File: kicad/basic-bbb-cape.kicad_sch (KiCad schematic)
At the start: 3 parts, among them J8 BBB_P8, J9 BBB_P9, U1 CAT24C32YI-GT3

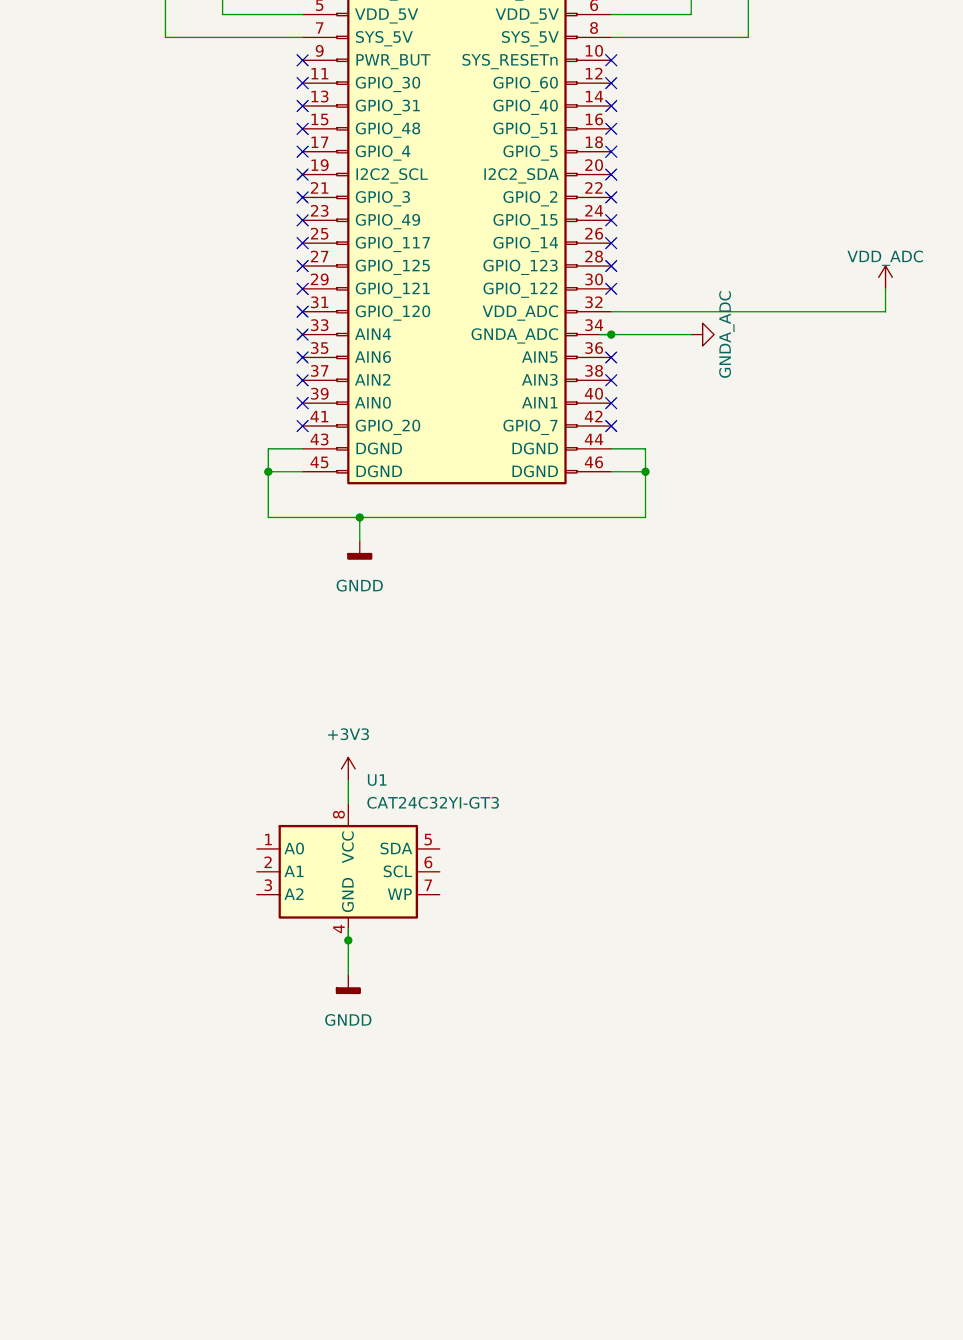
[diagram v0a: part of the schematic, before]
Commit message: Add resistor pack/network
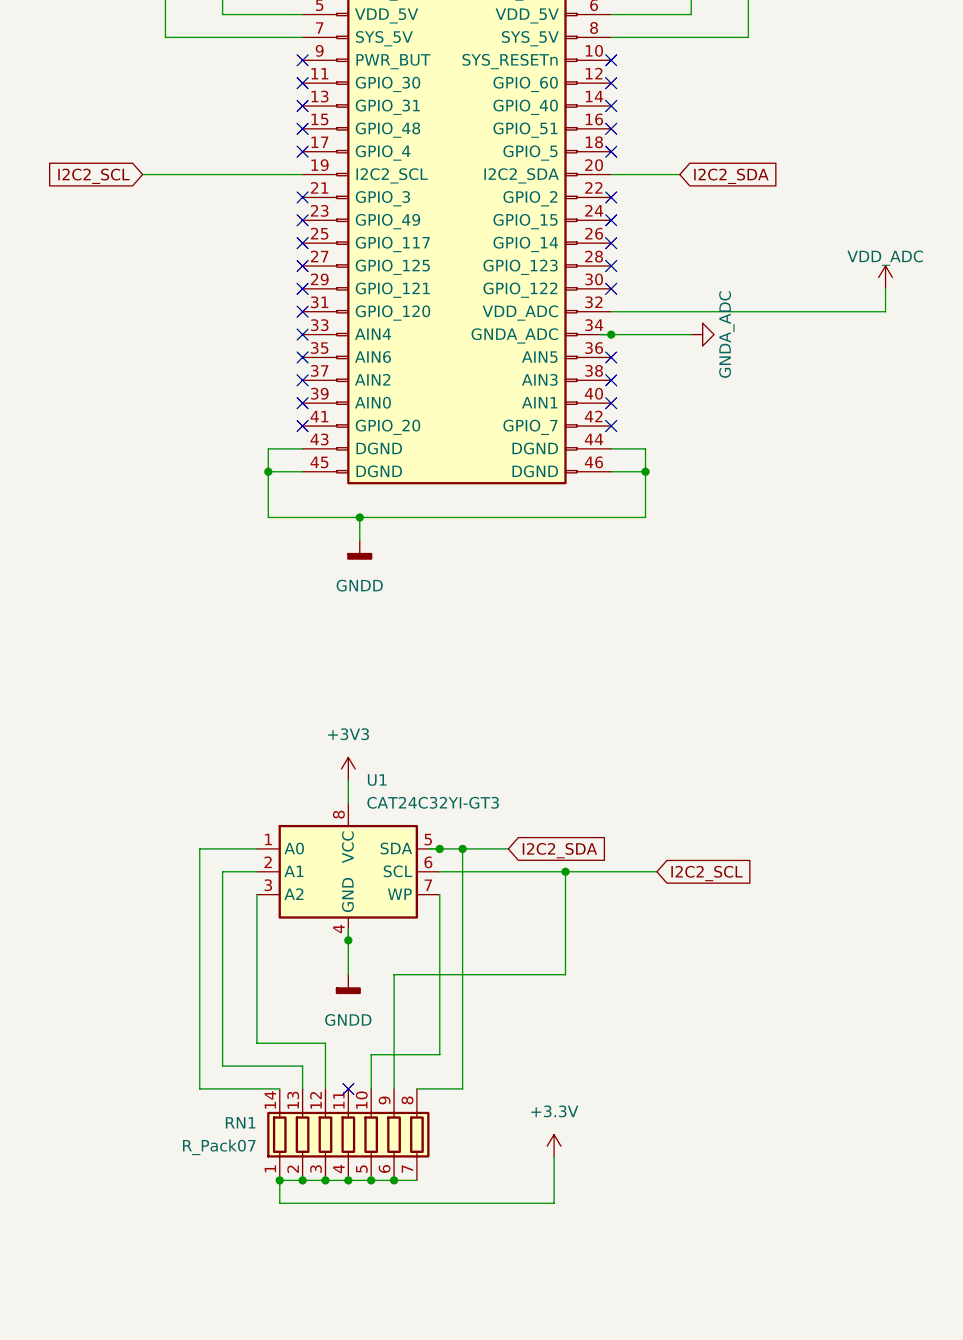
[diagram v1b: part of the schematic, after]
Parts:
- added RN1: R_Pack07, symbol Device:R_Pack07
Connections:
- net +3V3: now also RN1.1 (R1.1), RN1.2 (R2.1), RN1.3 (R3.1), RN1.4 (R4.1), RN1.5 (R5.1), RN1.6 (R6.1), RN1.7 (R7.1)
- net at U1.1 (A0): now also RN1.14 (R1.2)
- net at U1.2 (A1): now also RN1.13 (R2.2)
- net at U1.3 (A2): now also RN1.12 (R3.2)
- net I2C2_SDA: now reaches U1.5 (SDA)
- net I2C2_SDA: now also J9.20 (I2C2_SDA), RN1.8 (R7.2)
- net I2C2_SCL: now reaches U1.6 (SCL)
- net I2C2_SCL: now also J9.19 (I2C2_SCL), RN1.9 (R6.2)
- net at U1.7 (WP): now also RN1.10 (R5.2)
- no-connect marks 76 -> 75

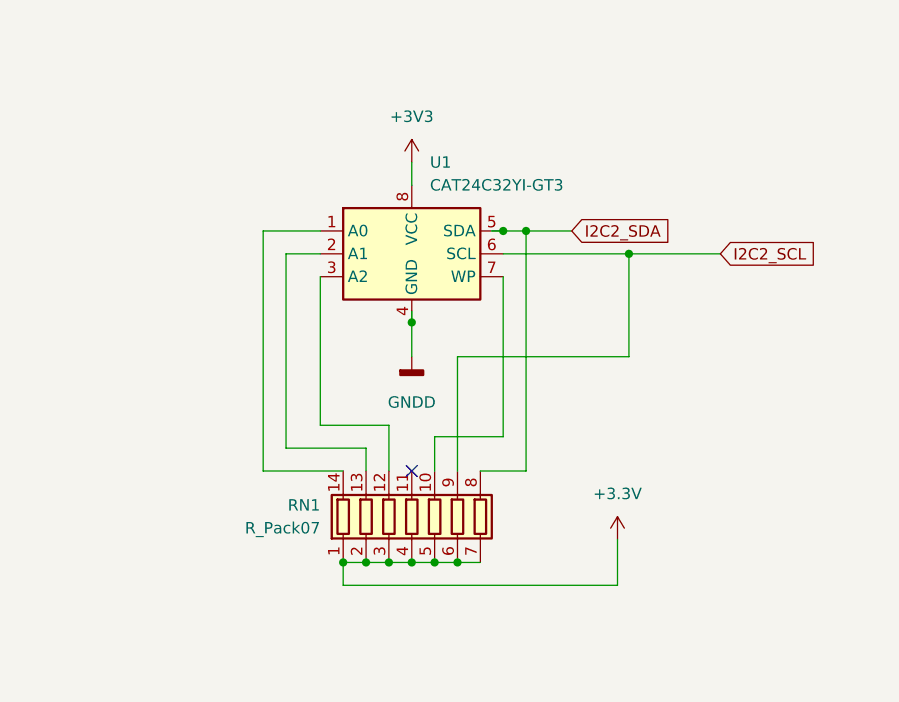
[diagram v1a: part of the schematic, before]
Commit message: Add Jumpers and test point
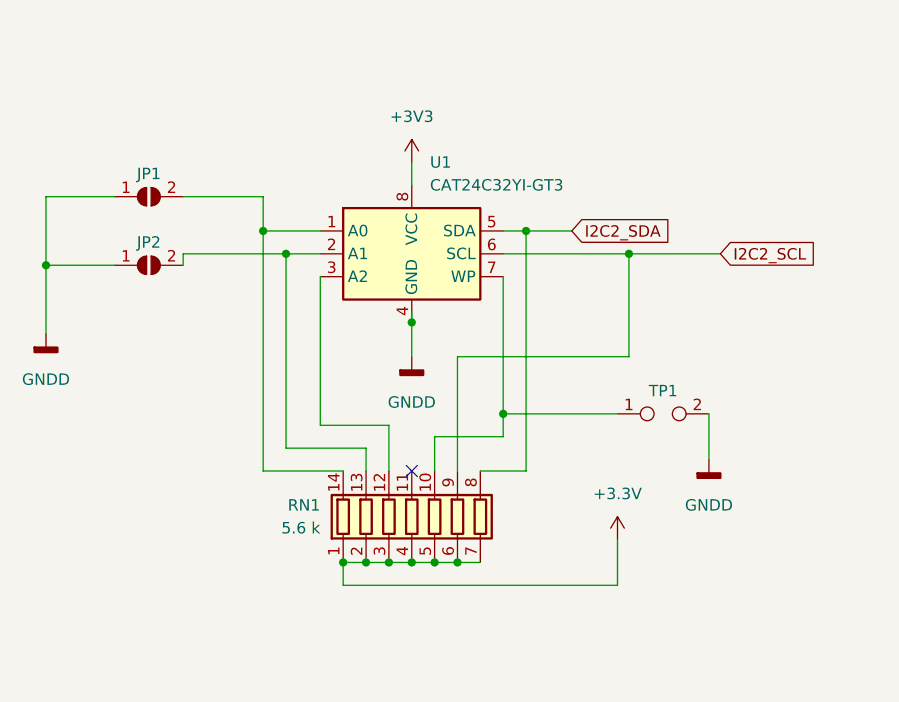
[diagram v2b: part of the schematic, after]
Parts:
- added JP1, JP2: SolderJumper_2_Open, symbol Jumper:SolderJumper_2_Open
- added TP1: TestPoint_2Pole, symbol Connector:TestPoint_2Pole
- RN1: value R_Pack07 -> 5.6 k
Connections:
- net GNDD: now also JP1.1 (A), JP2.1 (A), TP1.2
- net at RN1.14 (R1.2), U1.1 (A0): now also JP1.2 (B)
- net at RN1.13 (R2.2), U1.2 (A1): now also JP2.2 (B)
- net at RN1.10 (R5.2), U1.7 (WP): now also TP1.1
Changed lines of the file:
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@@
   (junction (at 60.96 163.83) (diameter 0) (color 0 0 0 0)
   )
+  (junction (at 63.5 163.83) (diameter 0) (color 0 0 0 0)
+  )
+  (junction (at 66.04 163.83) (diameter 0) (color 0 0 0 0)
+  )
+  (junction (at 93.98 85.09) (diameter 0) (color 0 0 0 0)
+  )
   (junction (at 73.66 127) (diameter 0) (color 0 0 0 0)
   )
-  (junction (at 63.5 163.83) (diameter 0) (color 0 0 0 0)
-  )
-  (junction (at 66.04 163.83) (diameter 0) (color 0 0 0 0)
-  )
-  (junction (at 93.98 85.09) (diameter 0) (color 0 0 0 0)
+  (junction (at 20.32 130.81) (diameter 0) (color 0 0 0 0)
   )
   (junction (at 53.34 163.83) (diameter 0) (color 0 0 0 0)
   )
+  (junction (at 71.12 147.32) (diameter 0) (color 0 0 0 0)
+  )
   (junction (at 85.09 129.54) (diameter 0) (color 0 0 0 0)
   )
@@
   (junction (at 55.88 163.83) (diameter 0) (color 0 0 0 0)
   )
-  (junction (at 71.12 127) (diameter 0) (color 0 0 0 0)
+  (junction (at 46.99 129.54) (diameter 0) (color 0 0 0 0)
+  )
+  (junction (at 44.45 127) (diameter 0) (color 0 0 0 0)
   )
   (junction (at 58.42 163.83) (diameter 0) (color 0 0 0 0)
@@
     (stroke (width 0) (type default) (color 0 0 0 0))
   )
-  (wire (pts (xy 71.12 149.86) (xy 71.12 132.08))
+  (wire (pts (xy 71.12 147.32) (xy 71.12 132.08))
+    (stroke (width 0) (type default) (color 0 0 0 0))
+  )
+  (wire (pts (xy 44.45 123.19) (xy 44.45 127))
+    (stroke (width 0) (type default) (color 0 0 0 0))
+  )
+  (wire (pts (xy 71.12 149.86) (xy 71.12 147.32))
     (stroke (width 0) (type default) (color 0 0 0 0))
   )
@@
     (stroke (width 0) (type default) (color 0 0 0 0))
   )
+  (wire (pts (xy 20.32 123.19) (xy 20.32 130.81))
+    (stroke (width 0) (type default) (color 0 0 0 0))
+  )
   (wire (pts (xy 83.82 161.29) (xy 83.82 166.37))
     (stroke (width 0) (type default) (color 0 0 0 0))
@@
     (stroke (width 0) (type default) (color 0 0 0 0))
   )
+  (wire (pts (xy 35.56 129.54) (xy 35.56 130.81))
+    (stroke (width 0) (type default) (color 0 0 0 0))
+  )
+  (wire (pts (xy 35.56 123.19) (xy 44.45 123.19))
+    (stroke (width 0) (type default) (color 0 0 0 0))
+  )
   (wire (pts (xy 52.07 82.55) (xy 55.88 82.55))
     (stroke (width 0) (type default) (color 0 0 0 0))
   )
-  (wire (pts (xy 69.85 127) (xy 71.12 127))
-    (stroke (width 0) (type default) (color 0 0 0 0))
-  )
   (wire (pts (xy 93.98 82.55) (xy 93.98 85.09))
     (stroke (width 0) (type default) (color 0 0 0 0))
@@
     (stroke (width 0) (type default) (color 0 0 0 0))
   )
+  (wire (pts (xy 20.32 130.81) (xy 20.32 138.43))
+    (stroke (width 0) (type default) (color 0 0 0 0))
+  )
   (wire (pts (xy 55.88 163.83) (xy 58.42 163.83))
     (stroke (width 0) (type default) (color 0 0 0 0))
@@
     (stroke (width 0) (type default) (color 0 0 0 0))
   )
+  (wire (pts (xy 20.32 130.81) (xy 27.94 130.81))
+    (stroke (width 0) (type default) (color 0 0 0 0))
+  )
   (wire (pts (xy 44.45 127) (xy 50.8 127))
     (stroke (width 0) (type default) (color 0 0 0 0))
   )
+  (wire (pts (xy 46.99 129.54) (xy 35.56 129.54))
+    (stroke (width 0) (type default) (color 0 0 0 0))
+  )
   (wire (pts (xy 90.17 31.75) (xy 93.98 31.75))
     (stroke (width 0) (type default) (color 0 0 0 0))
@@
     (stroke (width 0) (type default) (color 0 0 0 0))
   )
+  (wire (pts (xy 71.12 147.32) (xy 83.82 147.32))
+    (stroke (width 0) (type default) (color 0 0 0 0))
+  )
   (wire (pts (xy 63.5 163.83) (xy 66.04 163.83))
     (stroke (width 0) (type default) (color 0 0 0 0))
@@
     (stroke (width 0) (type default) (color 0 0 0 0))
   )
+  (wire (pts (xy 71.12 127) (xy 73.66 127))
+    (stroke (width 0) (type default) (color 0 0 0 0))
+  )
   (wire (pts (xy 34.29 29.21) (xy 55.88 29.21))
     (stroke (width 0) (type default) (color 0 0 0 0))
@@
     (stroke (width 0) (type default) (color 0 0 0 0))
   )
+  (wire (pts (xy 20.32 123.19) (xy 27.94 123.19))
+    (stroke (width 0) (type default) (color 0 0 0 0))
+  )
   (wire (pts (xy 90.17 82.55) (xy 93.98 82.55))
     (stroke (width 0) (type default) (color 0 0 0 0))
@@
     (stroke (width 0) (type default) (color 0 0 0 0))
   )
+  (wire (pts (xy 93.98 147.32) (xy 93.98 152.4))
+    (stroke (width 0) (type default) (color 0 0 0 0))
+  )
   (wire (pts (xy 44.45 127) (xy 44.45 153.67))
-    (stroke (width 0) (type default) (color 0 0 0 0))
-  )
-  (wire (pts (xy 71.12 127) (xy 73.66 127))
     (stroke (width 0) (type default) (color 0 0 0 0))
   )
@@
     (pin "1")
   )
+  (symbol (lib_id "power:GNDD") (at 20.32 138.43 0) (unit 1)
+    (in_bom yes) (on_board yes) (fields_autoplaced)
+    (property "Reference" "#PWR?" (id 0) (at 20.32 144.78 0)
+      (effects (font (size 1.27 1.27)) hide)
+    )
+    (property "Value" "GNDD" (id 1) (at 20.32 143.51 0))
+    (property "Footprint" "" (id 2) (at 20.32 138.43 0)
+      (effects (font (size 1.27 1.27)) hide)
+    )
+    (property "Datasheet" "" (id 3) (at 20.32 138.43 0)
+      (effects (font (size 1.27 1.27)) hide)
+    )
+    (pin "1")
+  )
   (symbol (lib_id "Memory_EEPROM:24LC32") (at 60.96 129.54 0) (unit 1)
     (in_bom yes) (on_board yes) (fields_autoplaced)
@@
     (pin "8")
   )
+  (symbol (lib_id "Jumper:SolderJumper_2_Open") (at 31.75 130.81 0) (unit 1)
+    (in_bom yes) (on_board yes)
+    (property "Reference" "JP2" (id 0) (at 31.75 128.27 0))
+    (property "Value" "SolderJumper_2_Open" (id 1) (at 31.75 127 0)
+      (effects (font (size 1.27 1.27)) hide)
+    )
+    (property "Footprint" "" (id 2) (at 31.75 130.81 0)
+      (effects (font (size 1.27 1.27)) hide)
+    )
+    (property "Datasheet" "~" (id 3) (at 31.75 130.81 0)
+      (effects (font (size 1.27 1.27)) hide)
+    )
+    (pin "1")
+    (pin "2")
+  )
   (symbol (lib_id "power:GNDD") (at 62.23 92.71 0) (unit 1)
     (in_bom yes) (on_board yes) (fields_autoplaced)
@@
       (effects (font (size 1.27 1.27)) (justify right))
     )
-    (property "Value" "R_Pack07" (id 1) (at 50.8 160.0199 0)
+    (property "Value" "5.6 k" (id 1) (at 50.8 160.0199 0)
       (effects (font (size 1.27 1.27)) (justify right))
     )
@@
     (pin "1")
   )
+  (symbol (lib_id "power:GNDD") (at 93.98 152.4 0) (unit 1)
+    (in_bom yes) (on_board yes) (fields_autoplaced)
+    (property "Reference" "#PWR?" (id 0) (at 93.98 158.75 0)
+      (effects (font (size 1.27 1.27)) hide)
+    )
+    (property "Value" "GNDD" (id 1) (at 93.98 157.48 0))
+    (property "Footprint" "" (id 2) (at 93.98 152.4 0)
+      (effects (font (size 1.27 1.27)) hide)
+    )
+    (property "Datasheet" "" (id 3) (at 93.98 152.4 0)
+      (effects (font (size 1.27 1.27)) hide)
+    )
+    (pin "1")
+  )
   (symbol (lib_id "power:GNDD") (at 110.49 29.21 90) (unit 1)
     (in_bom yes) (on_board yes) (fields_autoplaced)
@@
     )
     (pin "1")
+  )
+  (symbol (lib_id "Connector:TestPoint_2Pole") (at 88.9 147.32 0) (unit 1)
+    (in_bom yes) (on_board yes)
+    (property "Reference" "TP1" (id 0) (at 88.9 144.78 0))
+    (property "Value" "TestPoint_2Pole" (id 1) (at 88.9 143.51 0)
+      (effects (font (size 1.27 1.27)) hide)
+    )
+    (property "Footprint" "" (id 2) (at 88.9 147.32 0)
+      (effects (font (size 1.27 1.27)) hide)
+    )
+    (property "Datasheet" "~" (id 3) (at 88.9 147.32 0)
+      (effects (font (size 1.27 1.27)) hide)
+    )
+    (pin "1")
+    (pin "2")
+  )
+  (symbol (lib_id "Jumper:SolderJumper_2_Open") (at 31.75 123.19 0) (unit 1)
+    (in_bom yes) (on_board yes)
+    (property "Reference" "JP1" (id 0) (at 31.75 120.65 0))
+    (property "Value" "SolderJumper_2_Open" (id 1) (at 31.75 119.38 0)
+      (effects (font (size 1.27 1.27)) hide)
+    )
+    (property "Footprint" "" (id 2) (at 31.75 123.19 0)
+      (effects (font (size 1.27 1.27)) hide)
+    )
+    (property "Datasheet" "~" (id 3) (at 31.75 123.19 0)
+      (effects (font (size 1.27 1.27)) hide)
+    )
+    (pin "1")
+    (pin "2")
   )
   (sheet_instances
@@
       (reference "#PWR0116") (unit 1) (value "+3.3V") (footprint "")
     )
+    (path "/2992221d-2f52-4d6a-a3e2-2e90a8c32164"
+      (reference "#PWR?") (unit 1) (value "GNDD") (footprint "")
+    )
+    (path "/c49befc1-66ce-41c7-a52b-f7c7694b7c0c"
+      (reference "#PWR?") (unit 1) (value "GNDD") (footprint "")
+    )
     (path "/99c7ecaa-bb52-4945-b305-8fcf1296061f"
       (reference "J8") (unit 1) (value "BBB_P8") (footprint "Socket_BeagleBone_Black:Socket_BeagleBone_Black")
@@
       (reference "J9") (unit 1) (value "BBB_P9") (footprint "Socket_BeagleBone_Black:Socket_BeagleBone_Black")
     )
+    (path "/fe024c77-8b5d-48f2-aac3-fec332431e02"
+      (reference "JP1") (unit 1) (value "SolderJumper_2_Open") (footprint "")
+    )
+    (path "/311e7bbb-a30b-483f-9c86-e38e5c8c6715"
+      (reference "JP2") (unit 1) (value "SolderJumper_2_Open") (footprint "")
+    )
     (path "/5a7dfcd7-0335-4ce5-94ea-54b61d3b55cb"
-      (reference "RN1") (unit 1) (value "R_Pack07") (footprint "")
+      (reference "RN1") (unit 1) (value "5.6 k") (footprint "")
+    )
+    (path "/fdd66e0c-ae8b-426c-b2d8-bf497bf6a98d"
+      (reference "TP1") (unit 1) (value "TestPoint_2Pole") (footprint "")
     )
     (path "/30640f3e-01de-43bc-87ae-630424a499f6"

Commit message: Placed RP on PCB; do not like it best to turn 180 degrees.
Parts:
- RN1: footprint (none) -> Package_DIP:DIP-14_W7.62mm_Socket_LongPads
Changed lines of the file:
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@@
   (symbol (lib_id "power:GNDD") (at 20.32 138.43 0) (unit 1)
     (in_bom yes) (on_board yes) (fields_autoplaced)
-    (property "Reference" "#PWR?" (id 0) (at 20.32 144.78 0)
+    (property "Reference" "#PWR0117" (id 0) (at 20.32 144.78 0)
       (effects (font (size 1.27 1.27)) hide)
     )
@@
       (effects (font (size 1.27 1.27)) (justify right))
     )
-    (property "Footprint" "" (id 2) (at 73.025 158.75 90)
+    (property "Footprint" "Package_DIP:DIP-14_W7.62mm_Socket_LongPads" (id 2) (at 73.025 158.75 90)
       (effects (font (size 1.27 1.27)) hide)
     )
@@
   (symbol (lib_id "power:GNDD") (at 93.98 152.4 0) (unit 1)
     (in_bom yes) (on_board yes) (fields_autoplaced)
-    (property "Reference" "#PWR?" (id 0) (at 93.98 158.75 0)
+    (property "Reference" "#PWR0118" (id 0) (at 93.98 158.75 0)
       (effects (font (size 1.27 1.27)) hide)
     )
@@
     )
     (path "/2992221d-2f52-4d6a-a3e2-2e90a8c32164"
-      (reference "#PWR?") (unit 1) (value "GNDD") (footprint "")
+      (reference "#PWR0117") (unit 1) (value "GNDD") (footprint "")
     )
     (path "/c49befc1-66ce-41c7-a52b-f7c7694b7c0c"
-      (reference "#PWR?") (unit 1) (value "GNDD") (footprint "")
+      (reference "#PWR0118") (unit 1) (value "GNDD") (footprint "")
     )
     (path "/99c7ecaa-bb52-4945-b305-8fcf1296061f"
@@
     )
     (path "/5a7dfcd7-0335-4ce5-94ea-54b61d3b55cb"
-      (reference "RN1") (unit 1) (value "5.6 k") (footprint "")
+      (reference "RN1") (unit 1) (value "5.6 k") (footprint "Package_DIP:DIP-14_W7.62mm_Socket_LongPads")
     )
     (path "/fdd66e0c-ae8b-426c-b2d8-bf497bf6a98d"
